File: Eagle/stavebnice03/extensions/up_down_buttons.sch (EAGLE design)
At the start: 6 parts

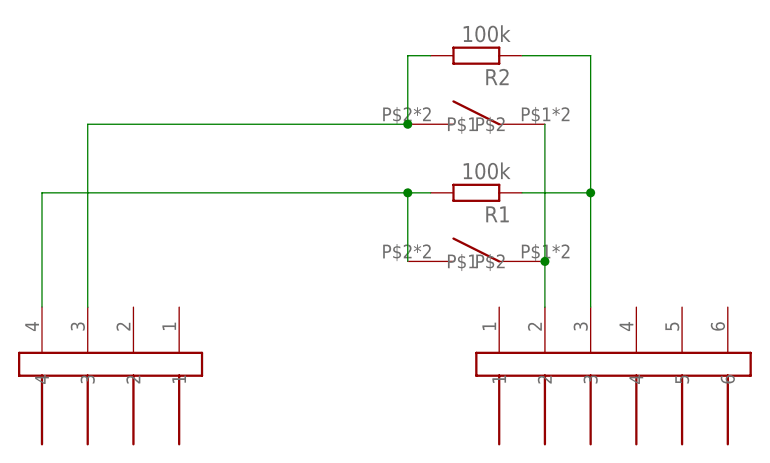
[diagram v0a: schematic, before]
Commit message: eagle adjustment for the Jíťa version
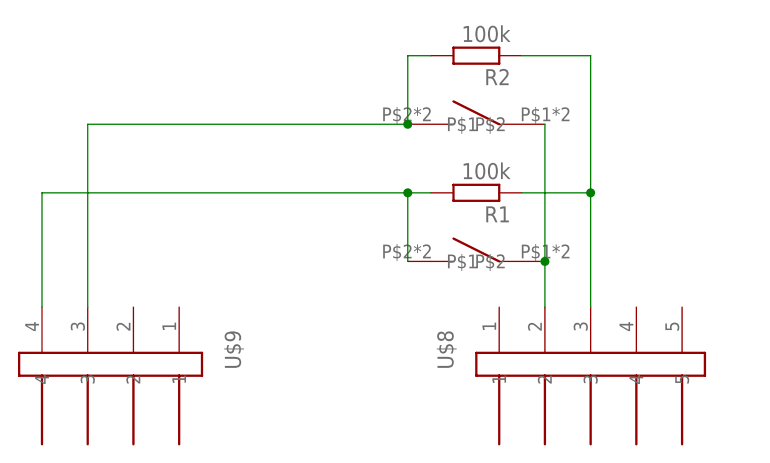
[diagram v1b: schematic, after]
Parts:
- U$8: value JUMPER6M -> JUMPER5M; device !stavebnice03:JUMPER6M -> !stavebnice03:JUMPER5M
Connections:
- net N$3 renamed GND
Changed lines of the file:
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@@
 </classes>
 <parts>
-<part name="U$8" library="!stavebnice03" deviceset="JUMPER6M" device=""/>
+<part name="U$8" library="!stavebnice03" deviceset="JUMPER5M" device=""/>
 <part name="U$9" library="!stavebnice03" deviceset="JUMPER4M" device=""/>
 <part name="R1" library="resistor" deviceset="R-EU_" device="R0603" value="100k"/>
@@
 </plain>
 <instances>
-<instance part="U$8" gate="G$1" x="175.26" y="35.56" rot="MR270"/>
+<instance part="U$8" gate="G$1" x="172.72" y="35.56" rot="MR270"/>
 <instance part="U$9" gate="G$1" x="119.38" y="35.56" rot="R270"/>
 <instance part="R1" gate="G$1" x="160.02" y="55.88" rot="R180"/>
@@
 </segment>
 </net>
-<net name="N$3" class="0">
+<net name="GND" class="0">
 <segment>
 <pinref part="R1" gate="G$1" pin="1"/>
